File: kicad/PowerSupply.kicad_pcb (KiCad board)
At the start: 2 copper layers, 93 x 116 mm, 112 parts, among them J1 USB_A, J2 Display, J3 USART, J4 Terminal, Q1 MMBT3904, Q2 MMBT3904, Q3 MMBT3904, Q4 MMBT3904, SW1 ENC0 (Voltage), SW2 ENC1 (Current)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

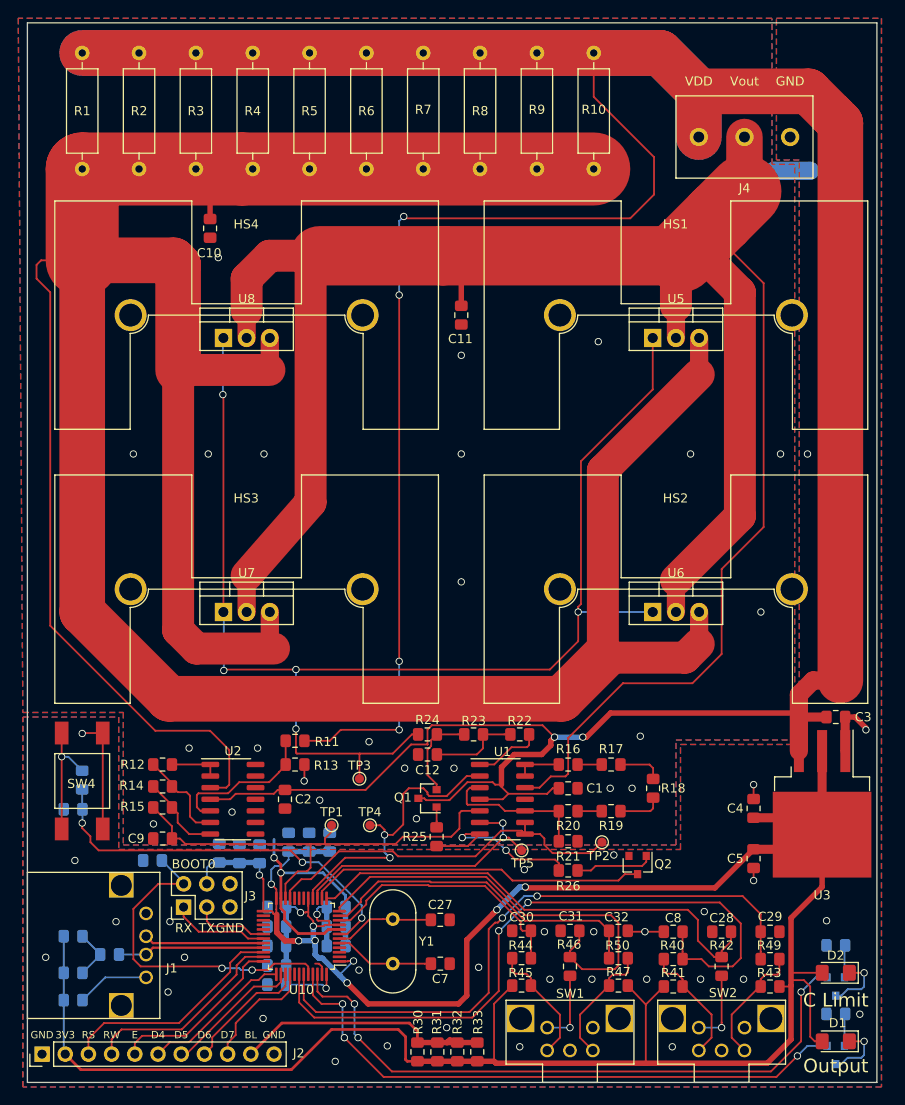
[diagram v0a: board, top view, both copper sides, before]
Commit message: Added a resistor to each gate of the pass transistors
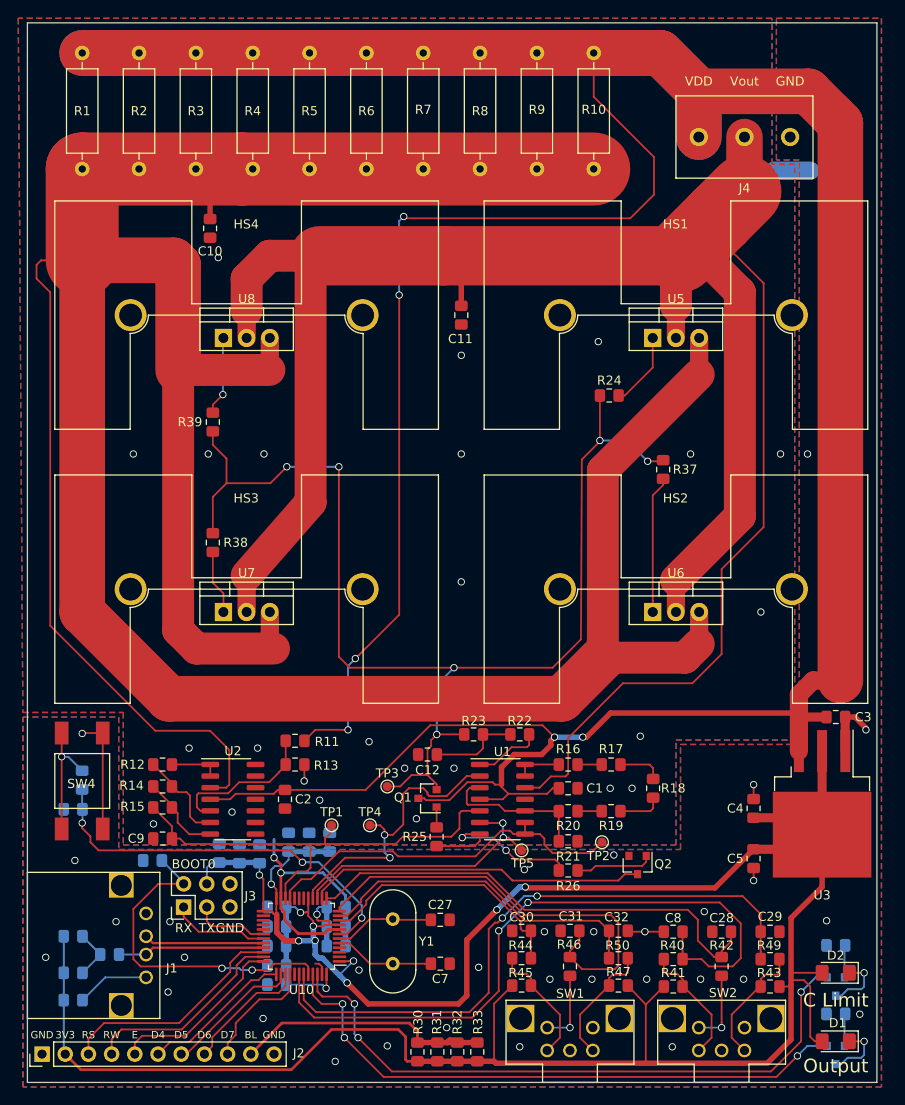
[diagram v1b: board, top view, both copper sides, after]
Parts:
- added R37: 100R, Resistor_SMD:R_0805_2012Metric_Pad1.15x1.40mm_HandSolder, F.Cu at (69.6, 48.9)
- added R38: 100R, Resistor_SMD:R_0805_2012Metric_Pad1.15x1.40mm_HandSolder, F.Cu at (20.3, 56.9)
- added R39: 100R, Resistor_SMD:R_0805_2012Metric_Pad1.15x1.40mm_HandSolder, F.Cu at (20.3, 43.7)
- R24: value ? -> 100R
- moved R24 42.1 mm to (63.7, 40.8)
- moved TP3 3.17 mm to (39.4, 83.6)
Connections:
- Q1 pad 2: Net-(Q1-Pad2) -> /PassElement/VReg_set
- R23 pad 1: Net-(Q1-Pad2) -> /PassElement/VReg_set
- R24 pad 2: Net-(Q1-Pad2) -> Net-(R24-Pad2)
- U5 pad 1: /PassElement/VReg_set -> Net-(R24-Pad2)
- U6 pad 1: /PassElement/VReg_set -> Net-(R37-Pad2)
- U7 pad 1: /PassElement/VReg_set -> Net-(R38-Pad1)
- U8 pad 1: /PassElement/VReg_set -> Net-(R39-Pad2)
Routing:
- net Net-(R37-Pad2): track 0.00 -> 15.0 mm
- net /PassElement/VReg_set: track 147.5 -> 132.9 mm, vias 5 -> 6
- net Net-(Q1-Pad2): track 9.89 -> 0.00 mm
- net Net-(R39-Pad2): track 0.00 -> 8.74 mm, vias 0 -> 1
- net Net-(R24-Pad2): track 0.00 -> 8.24 mm
- net Net-(R38-Pad1): track 0.00 -> 7.06 mm
- net VDD: track 454.6 -> 450.4 mm

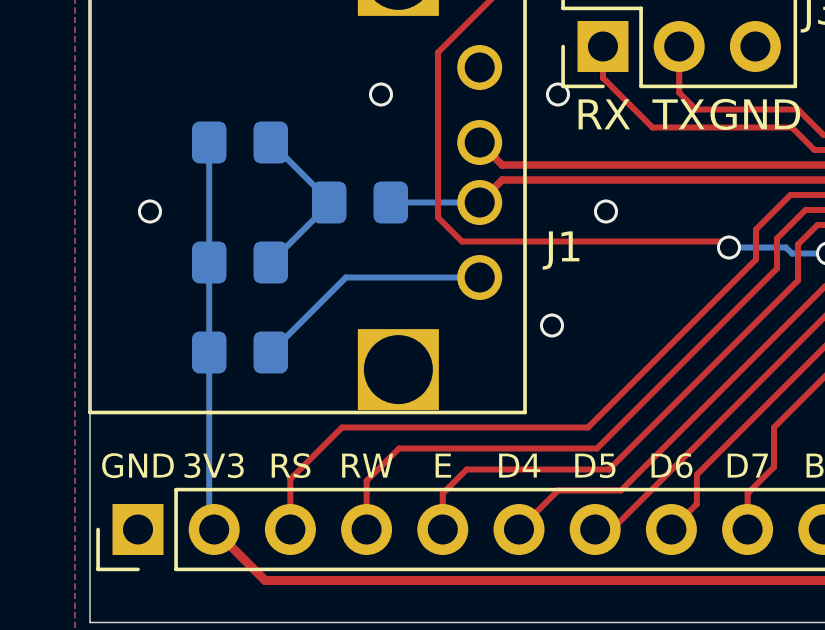
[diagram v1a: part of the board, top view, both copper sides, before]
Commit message: Removed unnecessary trace
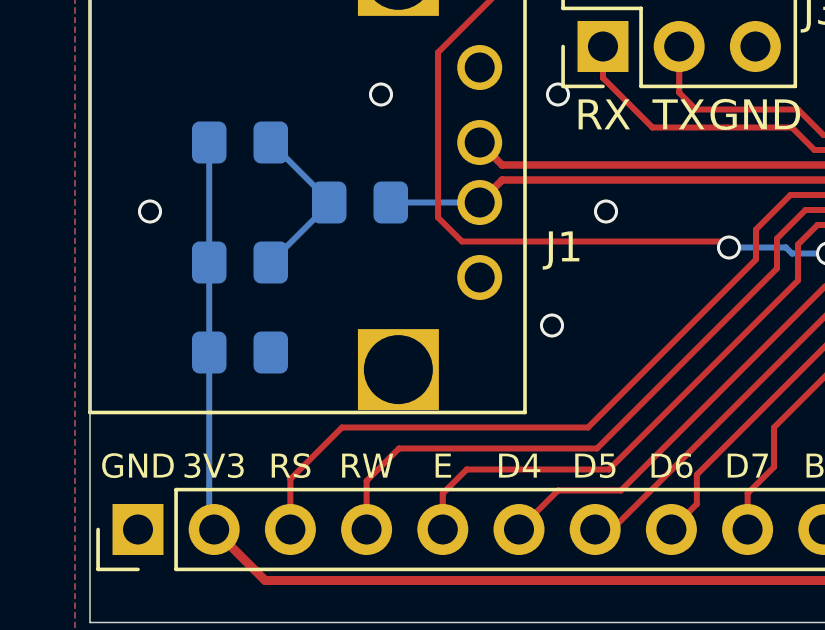
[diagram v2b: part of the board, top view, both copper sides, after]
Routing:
- net GNDREF: track 37.5 -> 29.5 mm
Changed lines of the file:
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@@
     (thickness 1.6)
     (drawings 24)
-    (tracks 895)
+    (tracks 893)
     (zones 0)
     (modules 115)
@@
   (segment (start 89.525 79.71) (end 89.54 79.725) (width 1) (layer F.Cu) (net 1))
   (segment (start 89.525 76) (end 89.525 79.71) (width 1) (layer F.Cu) (net 1))
-  (segment (start 8.525 104.5) (end 12.99 104.5) (width 0.2) (layer B.Cu) (net 1))
-  (segment (start 6.025 107) (end 8.525 104.5) (width 0.2) (layer B.Cu) (net 1))
   (segment (start 8.25 88.25) (end 8.25 77.75) (width 0.2) (layer F.Cu) (net 1))
   (via (at 6 77.8) (size 0.8) (drill 0.6) (layers F.Cu B.Cu) (net 1))
@@
   (segment (start 19.64 98.34) (end 19.64 96.8) (width 0.2) (layer F.Cu) (net 30))
   (segment (start 20.2 98.9) (end 19.64 98.34) (width 0.2) (layer F.Cu) (net 30))
-  (segment (start 44.8 83.35) (end 43.8 82.35) (width 0.2) (layer F.Cu) (net 48))
-  (segment (start 44.8 83.95) (end 44.8 83.35) (width 0.2) (layer F.Cu) (net 48))
   (segment (start 44.775 85.875) (end 44.8 85.85) (width 0.2) (layer F.Cu) (net 31))
   (segment (start 44.8 88.075) (end 44.8 85.85) (width 0.2) (layer F.Cu) (net 31))
@@
   (segment (start 53 79.3) (end 54.7 79.3) (width 0.2) (layer F.Cu) (net 47))
   (segment (start 54.7 79.3) (end 54.925 79.075) (width 0.2) (layer F.Cu) (net 47))
-  (via (at 21.4 40.7) (size 0.8) (drill 0.6) (layers F.Cu B.Cu) (net 79))
-  (segment (start 21.46 40.76) (end 21.4 40.7) (width 0.2) (layer F.Cu) (net 79))
-  (segment (start 21.4 34.56) (end 21.46 34.5) (width 0.2) (layer B.Cu) (net 79))
-  (segment (start 21.4 40.7) (end 21.4 34.56) (width 0.2) (layer B.Cu) (net 79))
+  (segment (start 44.8 83.35) (end 43.8 82.35) (width 0.2) (layer F.Cu) (net 48))
+  (segment (start 44.8 83.95) (end 44.8 83.35) (width 0.2) (layer F.Cu) (net 48))
   (segment (start 43.8 82.35) (end 42.05 82.35) (width 0.2) (layer F.Cu) (net 48))
   (segment (start 40.8 83.6) (end 39.4 83.6) (width 0.2) (layer F.Cu) (net 48))
@@
   (segment (start 20.3 57.925) (end 20.3 61.3) (width 0.2) (layer F.Cu) (net 78))
   (segment (start 20.3 61.3) (end 21.46 62.46) (width 0.2) (layer F.Cu) (net 78))
+  (via (at 21.4 40.7) (size 0.8) (drill 0.6) (layers F.Cu B.Cu) (net 79))
+  (segment (start 21.46 40.76) (end 21.4 40.7) (width 0.2) (layer F.Cu) (net 79))
+  (segment (start 21.4 34.56) (end 21.46 34.5) (width 0.2) (layer B.Cu) (net 79))
+  (segment (start 21.4 40.7) (end 21.4 34.56) (width 0.2) (layer B.Cu) (net 79))
   (segment (start 20.3 41.8) (end 21.4 40.7) (width 0.2) (layer F.Cu) (net 79))
   (segment (start 20.3 42.675) (end 20.3 41.8) (width 0.2) (layer F.Cu) (net 79))

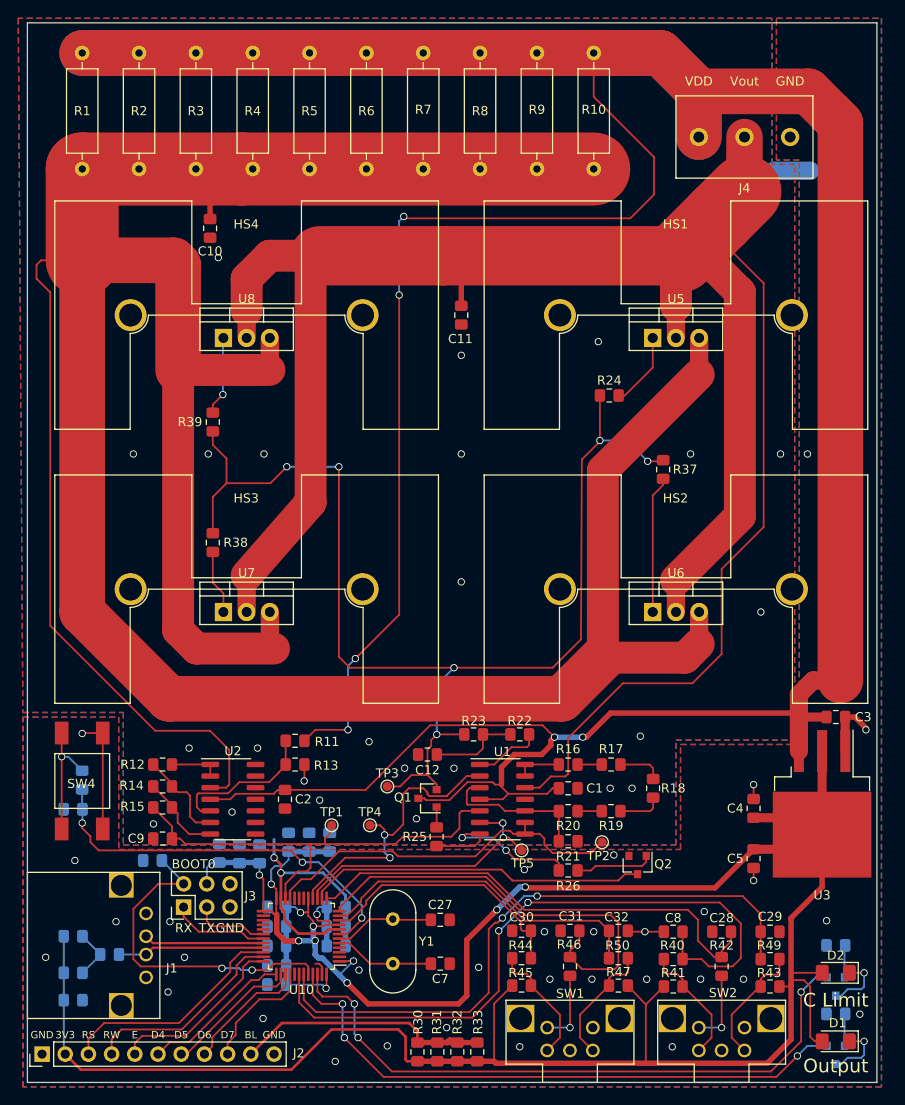
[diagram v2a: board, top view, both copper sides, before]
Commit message: Fixed wonky traces
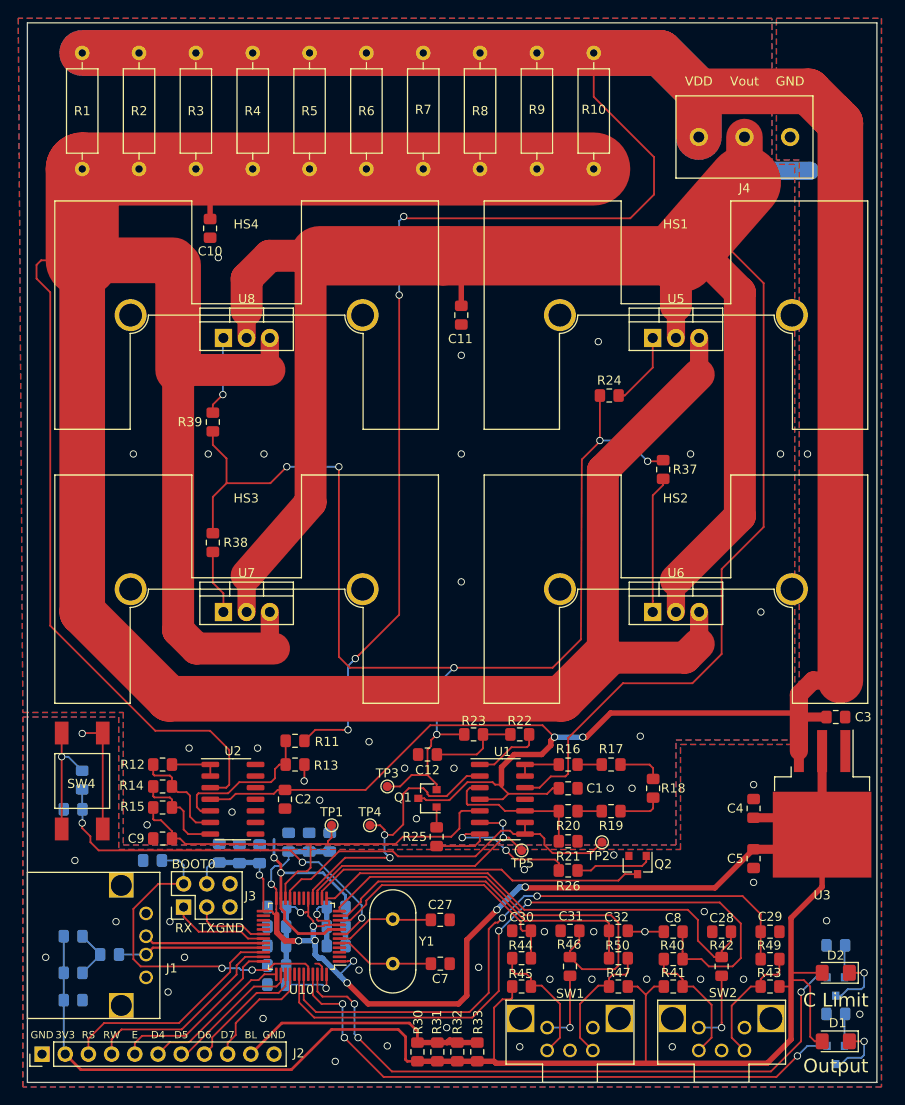
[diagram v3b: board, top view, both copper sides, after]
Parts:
- moved R45 0.10 mm to (54.1, 105.5)
- moved R47 0.10 mm to (64.7, 105.5)
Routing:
- net GNDREF: track 29.5 -> 19.9 mm, vias 32 -> 31
- net Net-(R14-Pad2): track 9.15 -> 11.1 mm
- net Net-(R12-Pad2): track 10.4 -> 11.8 mm
- net /Logic/BOOT0: track 36.6 -> 37.9 mm
- net Net-(R11-Pad2): track 16.5 -> 17.3 mm
- net /PassElement/Vin: track 384.5 -> 383.8 mm
- net Net-(R44-Pad1): track 13.6 -> 14.3 mm
- net Net-(R47-Pad2): track 13.7 -> 14.4 mm
- net /Vout: track 256.0 -> 256.7 mm
- net +3V3: track 317.8 -> 318.5 mm
- net Net-(R40-Pad1): track 13.5 -> 14.1 mm
- net Net-(R43-Pad2): track 13.6 -> 14.2 mm

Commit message: Tied unused opamps to ground as a voltage follower
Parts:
- C29, C30, C32, C6, C8: value 10n -> 10nF
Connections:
- U2 pad 10: (no net) -> GNDA
- U2 pad 12: (no net) -> GNDA
- U2 pad 13: (no net) -> Net-(U2-Pad13)
- U2 pad 14: (no net) -> Net-(U2-Pad13)
- U2 pad 8: (no net) -> Net-(U2-Pad8)
- U2 pad 9: (no net) -> Net-(U2-Pad8)
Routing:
- net Net-(U2-Pad8): track 0.00 -> 1.27 mm
- net Net-(U2-Pad13): track 0.00 -> 1.27 mm
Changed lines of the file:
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@@
     (thickness 1.6)
     (drawings 24)
-    (tracks 896)
+    (tracks 898)
     (zones 0)
     (modules 115)
-    (nets 80)
+    (nets 82)
   )
   (page A4)
@@
   (net 78 "Net-(R38-Pad1)")
   (net 79 "Net-(R39-Pad2)")
+  (net 80 "Net-(U2-Pad13)")
+  (net 81 "Net-(U2-Pad8)")
   (net_class Default "This is the default net class."
     (clearance 0.2)
@@
     (add_net "Net-(U10-Pad4)")
     (add_net "Net-(U10-Pad41)")
+    (add_net "Net-(U2-Pad13)")
+    (add_net "Net-(U2-Pad8)")
     (add_net VDD)
   )
@@
     (fp_line (start 0 4.435) (end -1.95 4.435) (layer F.SilkS) (width 0.12))
     (fp_line (start 0 4.435) (end 1.95 4.435) (layer F.SilkS) (width 0.12))
-    (pad 14 smd roundrect (at 2.475 -3.81) (size 1.95 0.6) (layers F.Cu F.Paste F.Mask) (roundrect_rratio 0.25))
-    (pad 13 smd roundrect (at 2.475 -2.54) (size 1.95 0.6) (layers F.Cu F.Paste F.Mask) (roundrect_rratio 0.25))
-    (pad 12 smd roundrect (at 2.475 -1.27) (size 1.95 0.6) (layers F.Cu F.Paste F.Mask) (roundrect_rratio 0.25))
+    (pad 14 smd roundrect (at 2.475 -3.81) (size 1.95 0.6) (layers F.Cu F.Paste F.Mask) (roundrect_rratio 0.25)
+      (net 80 "Net-(U2-Pad13)"))
+    (pad 13 smd roundrect (at 2.475 -2.54) (size 1.95 0.6) (layers F.Cu F.Paste F.Mask) (roundrect_rratio 0.25)
+      (net 80 "Net-(U2-Pad13)"))
+    (pad 12 smd roundrect (at 2.475 -1.27) (size 1.95 0.6) (layers F.Cu F.Paste F.Mask) (roundrect_rratio 0.25)
+      (net 75 GNDA))
     (pad 11 smd roundrect (at 2.475 0) (size 1.95 0.6) (layers F.Cu F.Paste F.Mask) (roundrect_rratio 0.25)
       (net 75 GNDA))
-    (pad 10 smd roundrect (at 2.475 1.27) (size 1.95 0.6) (layers F.Cu F.Paste F.Mask) (roundrect_rratio 0.25))
-    (pad 9 smd roundrect (at 2.475 2.54) (size 1.95 0.6) (layers F.Cu F.Paste F.Mask) (roundrect_rratio 0.25))
-    (pad 8 smd roundrect (at 2.475 3.81) (size 1.95 0.6) (layers F.Cu F.Paste F.Mask) (roundrect_rratio 0.25))
+    (pad 10 smd roundrect (at 2.475 1.27) (size 1.95 0.6) (layers F.Cu F.Paste F.Mask) (roundrect_rratio 0.25)
+      (net 75 GNDA))
+    (pad 9 smd roundrect (at 2.475 2.54) (size 1.95 0.6) (layers F.Cu F.Paste F.Mask) (roundrect_rratio 0.25)
+      (net 81 "Net-(U2-Pad8)"))
+    (pad 8 smd roundrect (at 2.475 3.81) (size 1.95 0.6) (layers F.Cu F.Paste F.Mask) (roundrect_rratio 0.25)
+      (net 81 "Net-(U2-Pad8)"))
     (pad 7 smd roundrect (at -2.475 3.81) (size 1.95 0.6) (layers F.Cu F.Paste F.Mask) (roundrect_rratio 0.25)
       (net 40 "Net-(R14-Pad2)"))
@@
       (effects (font (size 1 1) (thickness 0.15)))
     )
-    (fp_text value 10n (at 0 1.65) (layer F.Fab)
+    (fp_text value 10nF (at 0 1.65) (layer F.Fab)
       (effects (font (size 1 1) (thickness 0.15)))
     )
@@
       (effects (font (size 1 1) (thickness 0.15)))
     )
-    (fp_text value 10n (at 0 1.65) (layer F.Fab)
+    (fp_text value 10nF (at 0 1.65) (layer F.Fab)
       (effects (font (size 1 1) (thickness 0.15)))
     )
@@
       (effects (font (size 1 1) (thickness 0.15)))
     )
-    (fp_text value 10n (at 0 1.65) (layer F.Fab)
+    (fp_text value 10nF (at 0 1.65) (layer F.Fab)
       (effects (font (size 1 1) (thickness 0.15)))
     )
@@
       (effects (font (size 1 1) (thickness 0.15)))
     )
-    (fp_text value 10n (at 0 1.65) (layer F.Fab)
+    (fp_text value 10nF (at 0 1.65) (layer F.Fab)
       (effects (font (size 1 1) (thickness 0.15)))
     )
@@
       (effects (font (size 1 1) (thickness 0.15)) (justify mirror))
     )
-    (fp_text value 10n (at 0 -1.65) (layer B.Fab)
+    (fp_text value 10nF (at 0 -1.65) (layer B.Fab)
       (effects (font (size 1 1) (thickness 0.15)) (justify mirror))
     )
@@
   (segment (start 20.3 41.8) (end 21.4 40.7) (width 0.2) (layer F.Cu) (net 79))
   (segment (start 20.3 42.675) (end 20.3 41.8) (width 0.2) (layer F.Cu) (net 79))
+  (segment (start 24.975 82.46) (end 24.975 81.19) (width 0.2) (layer F.Cu) (net 80))
+  (segment (start 24.975 88.81) (end 24.975 87.54) (width 0.2) (layer F.Cu) (net 81))
   (zone (net 75) (net_name GNDA) (layer B.Cu) (hatch edge 0.508)
     (connect_pads (clearance 0.2))
